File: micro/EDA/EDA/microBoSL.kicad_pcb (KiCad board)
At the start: 4 copper layers, 40 x 13 mm, 37 parts, among them J1 Conn_01x04, J2 Conn_02x03_Odd_Even, J3 Conn_01x04, J4 Conn_01x04, J5 Conn_01x02, J6 Conn_01x10, J7 Conn_01x02, J8 USB_B_Micro, Q1 DMG2302UK, SW1 PTS636 SM43J SMTR LFS, U1 MAX40200ANS, U2 MAX40200ANS, U3 MCP1700-3302E_SOT23, U4 ATmega328-MMH, U5 MCP7940N-xSN, U6 74HC126PW-Q100, U7 FT232RQ, Y1 8MHz, Y2 32.768 kHz

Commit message: finished micro bosl design
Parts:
- moved U1 1.35 mm to (106.7, 111.4)
- moved U2 0.85 mm to (106.7, 108.0)
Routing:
- net A1: track 14.4 -> 6.04 mm
- net USB_V: track 17.9 -> 20.0 mm
- net V_3.3: track 67.1 -> 65.0 mm
- net Net-(U1-PadA2): track 7.15 -> 9.08 mm
- net GND: track 79.5 -> 81.0 mm
- net VPP: track 42.6 -> 43.6 mm
- net Net-(R6-Pad2): track 12.0 -> 12.8 mm
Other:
- rule trace_min: 0.16 -> 0
- board text added: "3V3"
- board text added: "A1"
- board text added: "A3"
- board text added: "CNT"
- board text added: "D10"
- board text added: "D11"
- board text added: "D12"
- board text added: "D13"
- board text added: "D3"
- board text added: "D4"
- board text added: "D7"
- board text added: "D8"
- board text added: "GND"
- board text added: "M-"
- board text added: "P"
- board text added: "RST"
- board text added: "RX"
- board text added: "S"
- board text added: "SCL"
- board text added: "SDA"
- board text added: "TX"
- board text added: "V+"
- board text added: "WKE"
- board text added: "microBoSL rev 0.1.0"

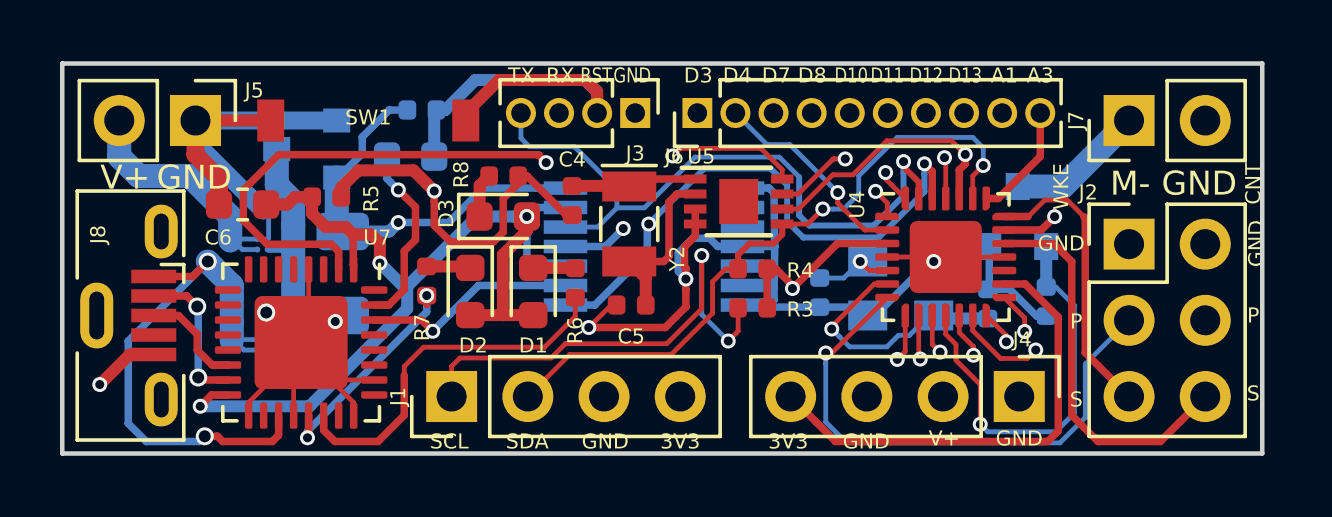
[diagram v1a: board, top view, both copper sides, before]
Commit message: changed some labled on microBoSL
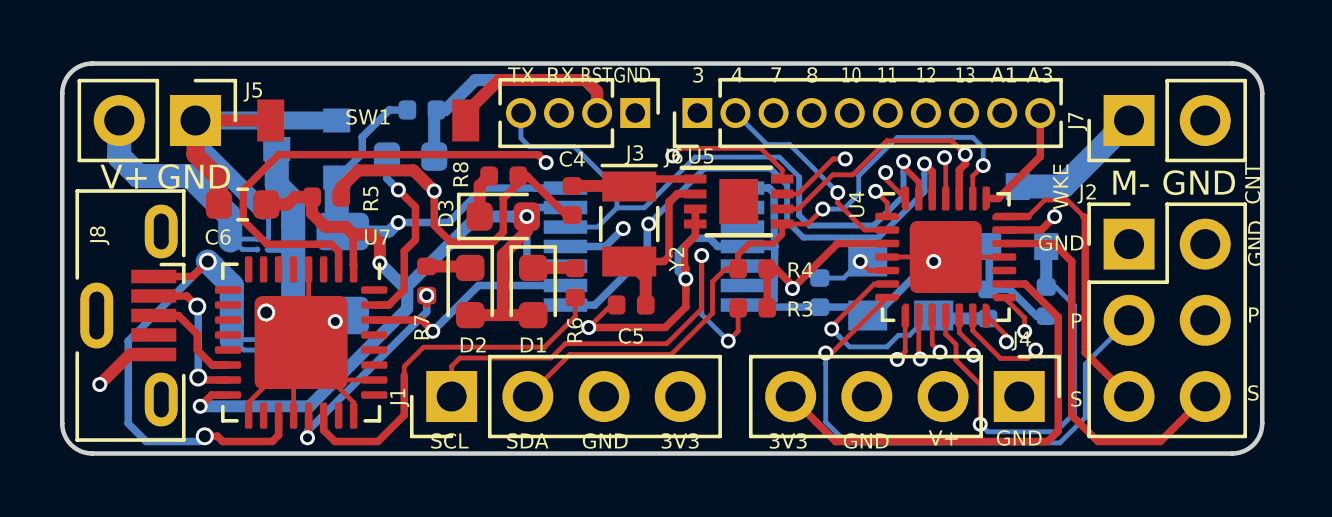
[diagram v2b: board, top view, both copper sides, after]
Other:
- outline, holes or cut-outs redrawn
- board text added: "10"
- board text added: "11"
- board text added: "12"
- board text added: "13"
- board text added: "3"
- board text added: "4"
- board text added: "7"
- board text added: "8"
- board text removed: "D10"
- board text removed: "D11"
- board text removed: "D12"
- board text removed: "D13"
- board text removed: "D3"
- board text removed: "D4"
- board text removed: "D7"
- board text removed: "D8"
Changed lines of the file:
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@@
   (general
     (thickness 1.6)
-    (drawings 39)
+    (drawings 77)
     (tracks 604)
     (zones 0)
@@
   )
   (setup
-    (last_trace_width 0.16)
+    (last_trace_width 0.25)
     (user_trace_width 0.16)
     (user_trace_width 0.2)
@@
     (solder_paste_margin 0.000001)
     (attr smd)
-    (fp_text reference U1 (at 0 0.975) (layer B.SilkS)
+    (fp_text reference U1 (at -1.185 0.105) (layer B.SilkS)
       (effects (font (size 0.5 0.5) (thickness 0.125)) (justify mirror))
     )
@@
     (solder_paste_margin 0.000001)
     (attr smd)
-    (fp_text reference U2 (at 0 1.025) (layer B.SilkS)
+    (fp_text reference U2 (at -1.085 0.245) (layer B.SilkS)
       (effects (font (size 0.5 0.5) (thickness 0.125)) (justify mirror))
     )
@@
     (tags SOT-23)
     (attr smd)
-    (fp_text reference Q1 (at -1.1 2.05 90) (layer B.SilkS)
+    (fp_text reference Q1 (at 1.28 -1.29 180) (layer B.SilkS)
       (effects (font (size 0.5 0.5) (thickness 0.125)) (justify mirror))
     )
@@
     )
   )
+  (gr_arc (start 139 114) (end 139 115) (angle -90) (layer Edge.Cuts) (width 0.15))
+  (gr_arc (start 101 114) (end 100 114) (angle -90) (layer Edge.Cuts) (width 0.15))
+  (gr_arc (start 101 103) (end 101 102) (angle -90) (layer Edge.Cuts) (width 0.15))
+  (gr_arc (start 139 103) (end 140 103) (angle -90) (layer Edge.Cuts) (width 0.15))
+  (gr_text V+ (at 102.1 105.83) (layer B.SilkS)
+    (effects (font (size 0.8 0.8) (thickness 0.15)) (justify mirror))
+  )
+  (gr_text GND (at 104.4 105.83) (layer B.SilkS)
+    (effects (font (size 0.8 0.8) (thickness 0.15)) (justify mirror))
+  )
+  (gr_text RX (at 116.63 102.37) (layer B.SilkS)
+    (effects (font (size 0.5 0.5) (thickness 0.125)) (justify mirror))
+  )
+  (gr_text 3 (at 121.23 102.37) (layer B.SilkS)
+    (effects (font (size 0.5 0.5) (thickness 0.125)) (justify mirror))
+  )
+  (gr_text 10 (at 126.33 102.37) (layer B.SilkS)
+    (effects (font (size 0.5 0.4) (thickness 0.1)) (justify mirror))
+  )
+  (gr_text 4 (at 122.53 102.37) (layer B.SilkS)
+    (effects (font (size 0.5 0.5) (thickness 0.125)) (justify mirror))
+  )
+  (gr_text 11 (at 127.53 102.37) (layer B.SilkS)
+    (effects (font (size 0.5 0.4) (thickness 0.1)) (justify mirror))
+  )
+  (gr_text A3 (at 132.63 102.37) (layer B.SilkS)
+    (effects (font (size 0.5 0.5) (thickness 0.125)) (justify mirror))
+  )
+  (gr_text RST (at 117.83 102.37) (layer B.SilkS)
+    (effects (font (size 0.5 0.4) (thickness 0.1)) (justify mirror))
+  )
+  (gr_text 13 (at 130.13 102.37) (layer B.SilkS)
+    (effects (font (size 0.5 0.4) (thickness 0.1)) (justify mirror))
+  )
+  (gr_text A1 (at 131.43 102.37) (layer B.SilkS)
+    (effects (font (size 0.5 0.5) (thickness 0.125)) (justify mirror))
+  )
+  (gr_text 8 (at 125.03 102.37) (layer B.SilkS)
+    (effects (font (size 0.5 0.5) (thickness 0.1)) (justify mirror))
+  )
+  (gr_text TX (at 115.33 102.37) (layer B.SilkS)
+    (effects (font (size 0.5 0.5) (thickness 0.125)) (justify mirror))
+  )
+  (gr_text GND (at 119.03 102.37) (layer B.SilkS)
+    (effects (font (size 0.5 0.4) (thickness 0.1)) (justify mirror))
+  )
+  (gr_text 7 (at 123.83 102.37) (layer B.SilkS)
+    (effects (font (size 0.5 0.5) (thickness 0.125)) (justify mirror))
+  )
+  (gr_text 12 (at 128.83 102.37) (layer B.SilkS)
+    (effects (font (size 0.5 0.4) (thickness 0.1)) (justify mirror))
+  )
+  (gr_text M- (at 135.63 106) (layer B.SilkS)
+    (effects (font (size 0.8 0.8) (thickness 0.15)) (justify mirror))
+  )
+  (gr_text GND (at 137.93 106) (layer B.SilkS)
+    (effects (font (size 0.8 0.8) (thickness 0.15)) (justify mirror))
+  )
+  (gr_text WKE (at 133.95 105.89 90) (layer B.SilkS)
+    (effects (font (size 0.5 0.5) (thickness 0.125)) (justify mirror))
+  )
+  (gr_text CNT (at 139.73 106 90) (layer B.SilkS)
+    (effects (font (size 0.5 0.5) (thickness 0.125)) (justify mirror))
+  )
+  (gr_text GND (at 133.91 107.99 90) (layer B.SilkS)
+    (effects (font (size 0.5 0.5) (thickness 0.125)) (justify mirror))
+  )
+  (gr_text GND (at 139.83 107.98 90) (layer B.SilkS)
+    (effects (font (size 0.5 0.5) (thickness 0.125)) (justify mirror))
+  )
+  (gr_text P (at 133.83 110.39) (layer B.SilkS)
+    (effects (font (size 0.5 0.5) (thickness 0.125)) (justify mirror))
+  )
+  (gr_text P (at 139.68 110.4) (layer B.SilkS)
+    (effects (font (size 0.5 0.5) (thickness 0.125)) (justify mirror))
+  )
+  (gr_text S (at 133.83 112.98) (layer B.SilkS)
+    (effects (font (size 0.5 0.5) (thickness 0.125)) (justify mirror))
+  )
+  (gr_text S (at 139.72 113) (layer B.SilkS)
+    (effects (font (size 0.5 0.5) (thickness 0.125)) (justify mirror))
+  )
+  (gr_text 3V3 (at 124.19 114.58) (layer B.SilkS)
+    (effects (font (size 0.5 0.5) (thickness 0.125)) (justify mirror))
+  )
+  (gr_text V+ (at 129.4 114.53) (layer B.SilkS)
+    (effects (font (size 0.5 0.5) (thickness 0.125)) (justify mirror))
+  )
+  (gr_text SCL (at 112.89 114.58) (layer B.SilkS)
+    (effects (font (size 0.5 0.5) (thickness 0.125)) (justify mirror))
+  )
+  (gr_text 3V3 (at 120.59 114.58) (layer B.SilkS)
+    (effects (font (size 0.5 0.5) (thickness 0.125)) (justify mirror))
+  )
+  (gr_text GND (at 118.09 114.58) (layer B.SilkS)
+    (effects (font (size 0.5 0.5) (thickness 0.125)) (justify mirror))
+  )
+  (gr_text GND (at 131.9 114.53) (layer B.SilkS)
+    (effects (font (size 0.5 0.5) (thickness 0.125)) (justify mirror))
+  )
+  (gr_text SDA (at 115.49 114.58) (layer B.SilkS)
+    (effects (font (size 0.5 0.5) (thickness 0.125)) (justify mirror))
+  )
+  (gr_text GND (at 126.79 114.58) (layer B.SilkS)
+    (effects (font (size 0.5 0.5) (thickness 0.125)) (justify mirror))
+  )
   (gr_text SCL (at 112.9 114.6) (layer F.SilkS)
     (effects (font (size 0.5 0.5) (thickness 0.125)))
@@
     (effects (font (size 0.5 0.5) (thickness 0.125)))
   )
-  (gr_text D13 (at 130.1 102.4) (layer F.SilkS)
+  (gr_text 13 (at 130.1 102.4) (layer F.SilkS)
     (effects (font (size 0.5 0.4) (thickness 0.1)))
   )
-  (gr_text D12 (at 128.8 102.4) (layer F.SilkS)
+  (gr_text 12 (at 128.8 102.4) (layer F.SilkS)
     (effects (font (size 0.5 0.4) (thickness 0.1)))
   )
-  (gr_text D11 (at 127.5 102.4) (layer F.SilkS)
+  (gr_text 11 (at 127.5 102.4) (layer F.SilkS)
     (effects (font (size 0.5 0.4) (thickness 0.1)))
   )
-  (gr_text D10 (at 126.3 102.4) (layer F.SilkS)
+  (gr_text 10 (at 126.3 102.4) (layer F.SilkS)
     (effects (font (size 0.5 0.4) (thickness 0.1)))
   )
-  (gr_text D8 (at 125 102.4) (layer F.SilkS)
+  (gr_text 8 (at 125 102.4) (layer F.SilkS)
     (effects (font (size 0.5 0.5) (thickness 0.1)))
   )
-  (gr_text D7 (at 123.8 102.4) (layer F.SilkS)
-    (effects (font (size 0.5 0.5) (thickness 0.125)))
-  )
-  (gr_text D4 (at 122.5 102.4) (layer F.SilkS)
-    (effects (font (size 0.5 0.5) (thickness 0.125)))
-  )
-  (gr_text D3 (at 121.2 102.4) (layer F.SilkS)
+  (gr_text 7 (at 123.8 102.4) (layer F.SilkS)
+    (effects (font (size 0.5 0.5) (thickness 0.125)))
+  )
+  (gr_text 4 (at 122.5 102.4) (layer F.SilkS)
+    (effects (font (size 0.5 0.5) (thickness 0.125)))
+  )
+  (gr_text 3 (at 121.2 102.4) (layer F.SilkS)
     (effects (font (size 0.5 0.5) (thickness 0.125)))
   )
@@
     (effects (font (size 0.8 0.8) (thickness 0.15)) (justify mirror))
   )
-  (gr_line (start 140 102) (end 100 102) (layer Edge.Cuts) (width 0.15))
-  (gr_line (start 140 115) (end 140 102) (layer Edge.Cuts) (width 0.15))
-  (gr_line (start 100 115) (end 140 115) (layer Edge.Cuts) (width 0.15))
-  (gr_line (start 100 102) (end 100 115) (layer Edge.Cuts) (width 0.15))
+  (gr_line (start 139 102) (end 101 102) (layer Edge.Cuts) (width 0.15))
+  (gr_line (start 140 114) (end 140 103) (layer Edge.Cuts) (width 0.15))
+  (gr_line (start 101 115) (end 139 115) (layer Edge.Cuts) (width 0.15))
+  (gr_line (start 100 103) (end 100 114) (layer Edge.Cuts) (width 0.15))
   (via (at 109.1 110.6) (size 0.5) (drill 0.3) (layers F.Cu B.Cu) (net 1))
   (segment (start 127.55 108.45) (end 129.45 108.45) (width 0.16) (layer F.Cu) (net 1))

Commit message: microbosl layout finished TODO: optimise/silkscreen
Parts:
- removed the C6 at (106.0, 106.7)
- removed the D3 at (114.7, 107.1)
- removed the J3 at (119.1, 103.7)
- removed the R2 at (132.8, 109.9)
- added C10: 100 nF, Capacitor_SMD:C_0402_1005Metric, F.Cu at (111.8, 109.2)
- added C11: 100 nF, Capacitor_SMD:C_0402_1005Metric, F.Cu at (111.8, 111.4)
- added C3: 100 nF, Capacitor_SMD:C_0402_1005Metric, F.Cu at (132.6, 103.8)
- added C4: 100 nF, Capacitor_SMD:C_0402_1005Metric, F.Cu at (126.8, 103.8)
- added D2: LED, LED_SMD:LED_0603_1608Metric, F.Cu at (115.3, 113.0)
- added J2: Conn_01x03, Connector_PinHeader_1.27mm:PinHeader_1x03_P1.27mm_Vertical, F.Cu at (119.9, 103.6)
- added R1: 10 kΩ, Resistor_SMD:R_0402_1005Metric, B.Cu at (107.2, 103.6)
- added R6: 4.7 MΩ, Capacitor_SMD:C_0402_1005Metric, B.Cu at (110.2, 103.6)
- added R9: 3.3 kΩ, Resistor_SMD:R_0402_1005Metric, F.Cu at (111.8, 113.4)
- added SW2: AYZ0103AGRLC, SIMFootprints:AYZ0103AGRLC, F.Cu at (111.4, 104.6)
- C1: value 1 μF -> 2.2 μF; footprint Capacitor_SMD:C_1206_3216Metric -> Capacitor_SMD:C_0805_2012Metric
- C5: renamed from C3; value 22 pF -> 15 pF
- C6: renamed from C2; value 22 pF -> 15 pF
- C7: footprint Capacitor_SMD:C_0603_1608Metric -> Capacitor_SMD:C_0402_1005Metric
- C8: renamed from C5; value 12 pF -> 15 pF
- C9: renamed from C4; value 12 pF -> 15 pF
- J1: footprint Connector_PinHeader_2.54mm:PinHeader_1x04_P2.54mm_Vertical -> Connector_PinHeader_1.27mm:PinHeader_1x04_P1.27mm_Vertical
- J4: renamed from J5; value Conn_01x02 -> BATTERY CONN
- J6: value Conn_01x10 -> Conn_01x04; footprint Connector_PinHeader_1.27mm:PinHeader_1x10_P1.27mm_Vertical -> Connector_PinHeader_1.27mm:PinHeader_1x04_P1.27mm_Vertical
- J7: value Conn_01x02 -> MOTOR_OUT
- Q1: value DMG2302UK -> DMP2165UW; footprint Package_TO_SOT_SMD:SOT-23 -> Package_TO_SOT_SMD:SOT-323_SC-70
- R5: value 10 kΩ -> 4.7 MΩ; footprint Resistor_SMD:R_0402_1005Metric -> Capacitor_SMD:C_0402_1005Metric; moved to B.Cu
- R7: value 3.3 kΩ -> 10 kΩ
- SW1: value PTS636 SM43J SMTR LFS -> RST_JMPR; footprint SIMFootprints:PTS636 SM43J SMTR LFS -> Jumper:SolderJumper-2_P1.3mm_Open_RoundedPad1.0x1.5mm
- U1, U2: value MAX40200ANS -> TPS709A33DBVT; footprint Package_BGA:WLP-4_0.73x0.73mm_Layout2x2_P0.35mm_Ball0.22mm_Pad0.2mm_NSMD -> Package_TO_SOT_SMD:SOT-23-5
- U3: value MCP1700-3302E_SOT23 -> ATmega328P-MMH; footprint Package_TO_SOT_SMD:SOT-23 -> Package_DFN_QFN:QFN-28-1EP_4x4mm_P0.45mm_EP2.4x2.4mm; moved to F.Cu
- U4: value ATmega328-MMH -> ZXBM5210-S; footprint Package_DFN_QFN:QFN-28-1EP_4x4mm_P0.45mm_EP2.4x2.4mm -> Package_SO:SOIC-8_3.9x4.9mm_P1.27mm; moved to B.Cu
- Y1: footprint Crystal:Crystal_SMD_EuroQuartz_MT-4Pin_3.2x2.5mm -> Crystal:Crystal_SMD_5032-2Pin_5.0x3.2mm
- Y2: footprint Crystal:Crystal_SMD_EuroQuartz_EQ161-2Pin_3.2x1.5mm -> Crystal:Crystal_SMD_2012-2Pin_2.0x1.2mm
- moved Q1 25.3 mm to (106.6, 107.2), turned to 180 degrees
- moved U3 21.6 mm to (129.4, 108.5), turned to 0 degrees
- moved SW1 20.0 mm to (130.2, 103.8)
- moved R5 4.74 mm to (112.6, 103.6), turned to 270 degrees
- moved J1 4.42 mm to (117.4, 113.2)
- moved U2 4.33 mm to (111.0, 107.8), turned to 90 degrees
- moved J6 3.77 mm to (124.9, 103.6), turned to 270 degrees
- moved R2 3.61 mm to (115.6, 103.7), turned to 90 degrees
- moved C1 3.60 mm to (111.0, 112.2), turned to 180 degrees
- moved U4 3.47 mm to (129.8, 105.0)
- moved D3 3.43 mm to (113.5, 113.0)
- moved R10 3.18 mm to (115.7, 108.8)
- moved C6 2.76 mm to (133.6, 109.7)
- moved C9 2.18 mm to (119.0, 105.7), turned to 0 degrees
- moved D1 1.64 mm to (114.4, 110.6), turned to 180 degrees
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- renumbered D2 to D3, J4 to J3, J2 to J5, R8 to R10, R1 to R2, R4 to R3, R3 to R4, R6 to R8, U6 to U5, U5 to U6
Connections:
- C5 pad 2: Net-(C3-Pad2) -> Net-(C5-Pad2)
- C6 pad 2: Net-(C2-Pad2) -> Net-(C6-Pad2)
- C7 pad 1: TLL_RST -> Net-(C7-Pad1)
- C7 pad 2: Net-(C7-Pad2) -> GND
- D3 pad 1: Net-(D2-Pad1) -> Net-(D3-Pad1)
- J3 pad 2: VPP -> VBAT
- J5 pad 3: Hall_WKE_P -> Hall_WKE_S
- J5 pad 4: Hall_CNT_P -> Hall_CNT_S
- J5 pad 5: Hall_WKE_S -> Hall_WKE_P
- J5 pad 6: Hall_CNT_S -> Hall_CNT_P
- J6 pad 1: D3 -> SCLK
- J6 pad 2: D4 -> MISO
- J6 pad 3: D7 -> MOSI
- J6 pad 4: D8 -> SS
- J7 pad 2: GND -> Net-(J7-Pad2)
- Q1 pad 1: MOSFET -> Net-(Q1-Pad1)
- Q1 pad 2: GND -> VBAT
- Q1 pad 3: Net-(J7-Pad1) -> VPP
- R10 pad 1: Net-(D3-Pad1) -> Net-(D1-Pad1)
- R5 pad 1: TTL_3.3V -> VPP
- R5 pad 2: GND -> Net-(C7-Pad1)
- R7 pad 1: Net-(D2-Pad1) -> TTL_3.3V
- R7 pad 2: Net-(R7-Pad2) -> GND
- R8 pad 1: Net-(D1-Pad1) -> Net-(D2-Pad1)
- U3 pad 1: GND -> D3
- U3 pad 2: V_3.3 -> D4
- U3 pad 3: Net-(U1-PadA2) -> V_3.3
- U4 pad 1: D3 -> Net-(J7-Pad1)
- U4 pad 2: D4 -> VBAT
- U4 pad 4: GND -> MFWD
- U4 pad 5: Net-(C3-Pad2) -> MREV
- U4 pad 6: Net-(C2-Pad2) -> V_3.3
- U4 pad 7: Hall_WKE_P -> Net-(J7-Pad2)
- U4 pad 8: Hall_CNT_P -> GND
- U6 pad 3: GND -> Net-(C7-Pad1)
- U6 pad 9: (no net) -> GND
- U7 pad 21: Net-(R7-Pad2) -> Net-(R9-Pad2)
- U7 pad 31: Net-(C7-Pad2) -> Net-(C11-Pad2)
- Y1 pad 1: Net-(C2-Pad2) -> Net-(C6-Pad2)
- Y1 pad 2: GND -> Net-(C5-Pad2)
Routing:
- net VBAT: track 0.00 -> 43.3 mm, vias 0 -> 1
- net VPP: track 43.6 -> 17.8 mm
- net MISO: track 0.00 -> 21.6 mm, vias 0 -> 2
- net SS: track 0.00 -> 21.2 mm, vias 0 -> 1
- net Net-(C7-Pad1): track 0.00 -> 20.1 mm, vias 0 -> 1
- net SCLK: track 0.00 -> 19.1 mm, vias 0 -> 2
- net MOSI: track 0.00 -> 16.4 mm, vias 0 -> 2
- net SCL: track 35.5 -> 19.3 mm
- net D11: track 15.0 -> 0.00 mm, vias 1 -> 0
- net Net-(C6-Pad2): track 0.00 -> 14.8 mm, vias 0 -> 2
- net MFWD: track 0.00 -> 13.9 mm, vias 0 -> 2
- net MOSFET: track 13.7 -> 0.00 mm, vias 1 -> 0
- net D10: track 13.1 -> 0.00 mm, vias 1 -> 0
- net MREV: track 0.00 -> 12.5 mm, vias 0 -> 2
- net D7: track 12.3 -> 0.00 mm, vias 1 -> 0
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
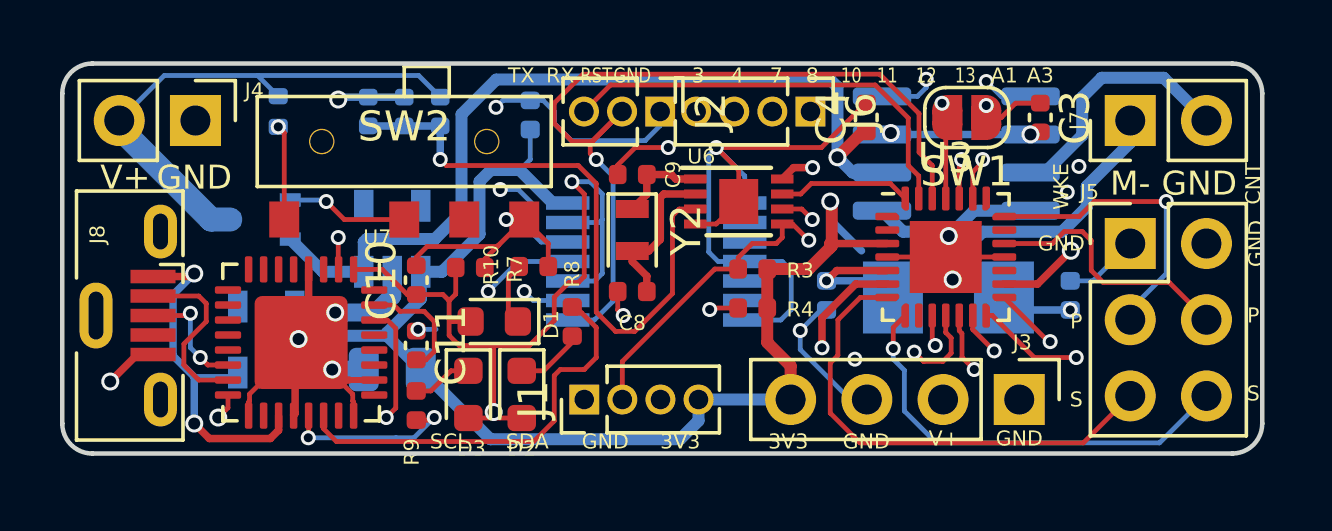
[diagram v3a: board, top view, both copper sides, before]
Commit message: optimised tracing on  micro
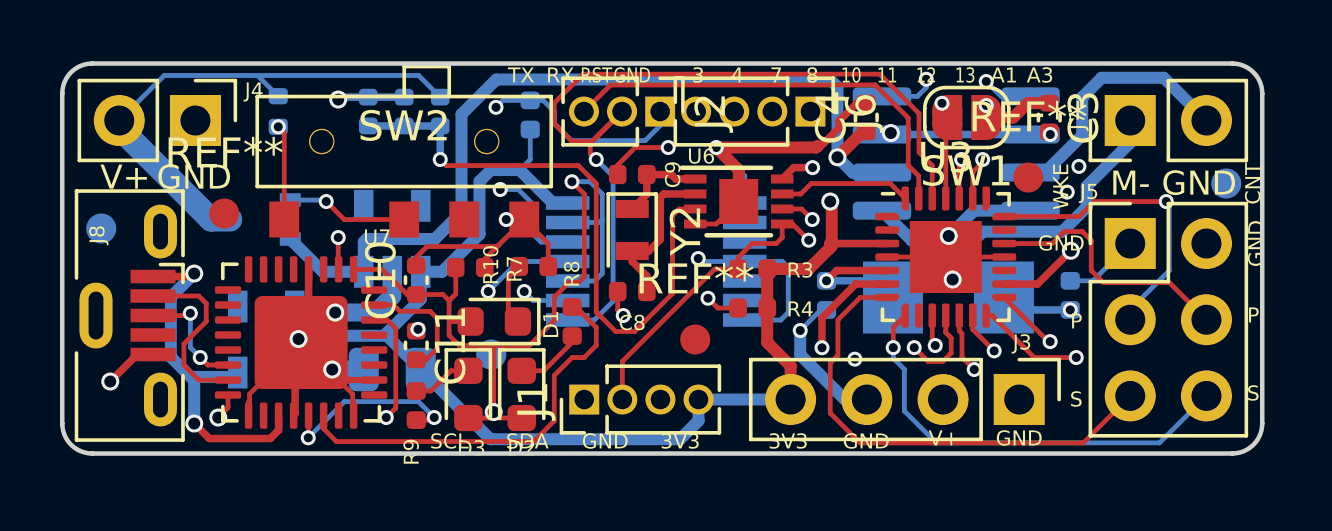
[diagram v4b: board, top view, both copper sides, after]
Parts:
- added REF**: Fiducial_1mm_Mask2mm, Fiducial:Fiducial_1mm_Mask2mm, B.Cu at (138.8, 106.0)
- added REF**: Fiducial_1mm_Mask2mm, Fiducial:Fiducial_1mm_Mask2mm, B.Cu at (101.3, 107.5)
- added REF**: Fiducial_1mm_Mask2mm, Fiducial:Fiducial_1mm_Mask2mm, B.Cu at (114.3, 111.7)
- added REF**: Fiducial_1mm_Mask2mm, Fiducial:Fiducial_1mm_Mask2mm, F.Cu at (132.2, 105.8)
- added REF**: Fiducial_1mm_Mask2mm, Fiducial:Fiducial_1mm_Mask2mm, F.Cu at (121.1, 111.2)
- added REF**: Fiducial_1mm_Mask2mm, Fiducial:Fiducial_1mm_Mask2mm, F.Cu at (105.4, 107.0)
- moved C3 0.30 mm to (132.9, 103.8)
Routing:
- net V_3.3: track 63.8 -> 60.9 mm
- net GND: track 73.8 -> 70.9 mm, vias 13 -> 14
